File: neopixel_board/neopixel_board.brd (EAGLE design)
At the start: 94 x 86 mm, 64 parts, among them U1 UA7805CKCT, U2 MIC5219, U3 ATMEGA32U4, U4 UA7805CKCT, U5 UA7805CKCT, U6 UA7805CKCT, Y1 16MHz

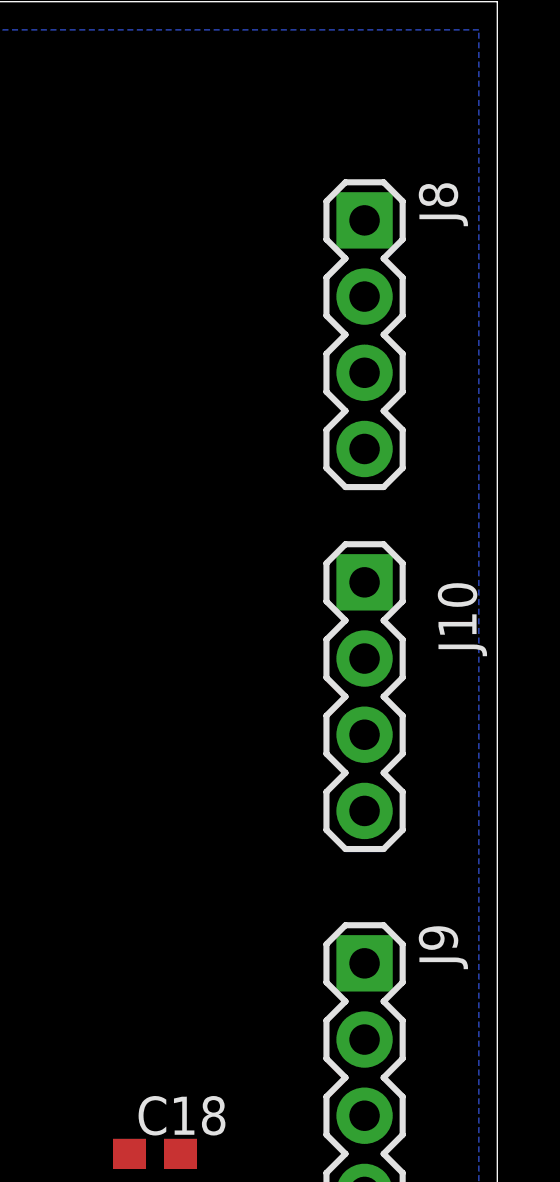
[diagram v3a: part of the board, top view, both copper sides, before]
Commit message: Schematic changes
Named neopixel connectors in order
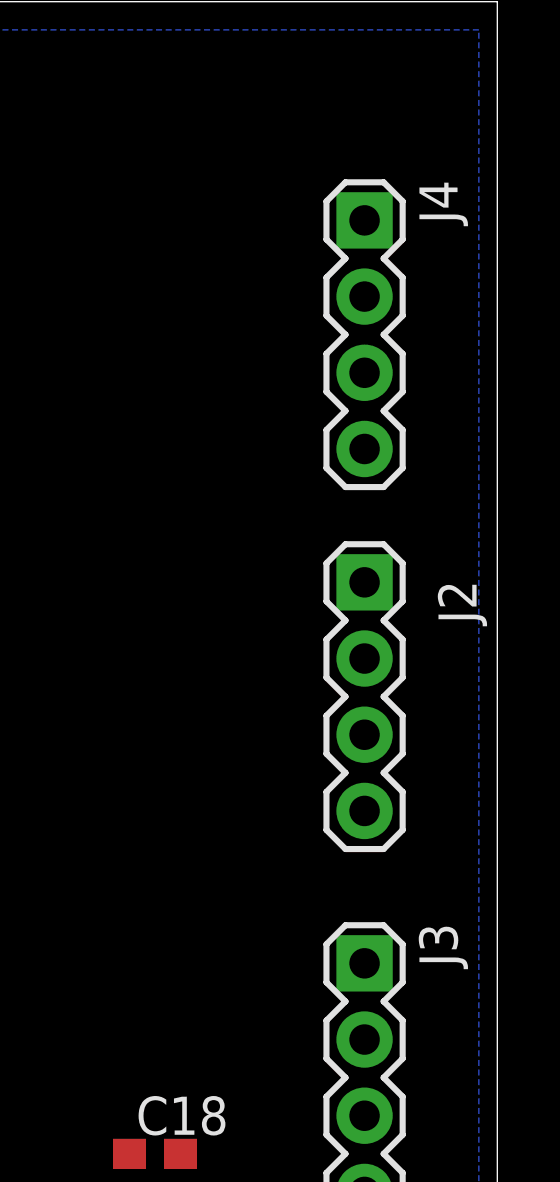
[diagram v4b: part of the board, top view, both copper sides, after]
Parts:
- renumbered J10 to J2, J8 to J4, J9 to J3
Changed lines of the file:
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@@
 <attribute name="VALUE" x="73.406" y="38.989" size="0.4064" layer="27"/>
 </element>
-<element name="J10" library="SparkFun-Connectors" package="1X04" value="" x="89.535" y="66.675" rot="R270">
+<element name="J2" library="SparkFun-Connectors" package="1X04" value="" x="89.535" y="66.675" rot="R270">
 <attribute name="NAME" x="91.9988" y="66.7512" size="1.27" layer="25" ratio="10" rot="R270"/>
 <attribute name="PROD_ID" value="CONN-09696" x="48.895" y="8.255" size="1.778" layer="27" rot="R270" display="off"/>
 <attribute name="VALUE" x="86.36" y="67.945" size="1.27" layer="27" rot="R270"/>
 </element>
-<element name="J8" library="SparkFun-Connectors" package="1X04" value="" x="89.535" y="78.74" rot="R270">
+<element name="J4" library="SparkFun-Connectors" package="1X04" value="" x="89.535" y="78.74" rot="R270">
 <attribute name="NAME" x="91.3638" y="80.0862" size="1.27" layer="25" ratio="10" rot="R270"/>
 <attribute name="PROD_ID" value="CONN-09696" x="48.895" y="43.18" size="1.778" layer="27" rot="R270" display="off"/>
 <attribute name="VALUE" x="86.36" y="80.01" size="1.27" layer="27" rot="R270"/>
 </element>
-<element name="J9" library="SparkFun-Connectors" package="1X04" value="" x="89.535" y="53.975" rot="R270">
+<element name="J3" library="SparkFun-Connectors" package="1X04" value="" x="89.535" y="53.975" rot="R270">
 <attribute name="NAME" x="91.3638" y="55.3212" size="1.27" layer="25" ratio="10" rot="R270"/>
 <attribute name="PROD_ID" value="CONN-09696" x="48.895" y="6.985" size="1.778" layer="27" rot="R270" display="off"/>
@@
 <contactref element="PB1" pad="P$3"/>
 <contactref element="PB1" pad="P$4"/>
-<contactref element="J10" pad="1"/>
-<contactref element="J8" pad="2"/>
-<contactref element="J10" pad="2"/>
-<contactref element="J9" pad="2"/>
-<contactref element="J9" pad="1"/>
-<contactref element="J8" pad="1"/>
+<contactref element="J2" pad="1"/>
+<contactref element="J4" pad="2"/>
+<contactref element="J2" pad="2"/>
+<contactref element="J3" pad="2"/>
+<contactref element="J3" pad="1"/>
+<contactref element="J4" pad="1"/>
 <contactref element="C2" pad="2"/>
 <contactref element="C4" pad="2"/>
@@
 </signal>
 <signal name="VCC2">
-<contactref element="J10" pad="4"/>
+<contactref element="J2" pad="4"/>
 <contactref element="U4" pad="3"/>
 <contactref element="C12" pad="1"/>
@@
 <contactref element="U5" pad="3"/>
 <contactref element="C15" pad="1"/>
-<contactref element="J9" pad="4"/>
+<contactref element="J3" pad="4"/>
 <contactref element="R9" pad="1"/>
 <contactref element="C21" pad="1"/>
@@
 </signal>
 <signal name="VCC4">
-<contactref element="J8" pad="4"/>
+<contactref element="J4" pad="4"/>
 <contactref element="R10" pad="1"/>
 <contactref element="U6" pad="3"/>
@@
 <signal name="N$14">
 <contactref element="R12" pad="1"/>
-<contactref element="J10" pad="3"/>
+<contactref element="J2" pad="3"/>
 <wire x1="89.535" y1="61.595" x2="63.92" y2="31.115" width="0" layer="19" extent="1-1"/>
 </signal>
 <signal name="N$15">
 <contactref element="R13" pad="1"/>
-<contactref element="J9" pad="3"/>
+<contactref element="J3" pad="3"/>
 <wire x1="89.535" y1="48.895" x2="67.095" y2="77.47" width="0" layer="19" extent="1-1"/>
 </signal>
@@
 <signal name="N$3">
 <contactref element="R14" pad="1"/>
-<contactref element="J8" pad="3"/>
+<contactref element="J4" pad="3"/>
 <wire x1="89.535" y1="73.66" x2="63.285" y2="77.47" width="0" layer="19" extent="1-1"/>
 </signal>

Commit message: Board Finished (tentative)
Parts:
- removed C1: 0.1uF, rcl:C0603
- removed C11, C14, C16, C8: 0.1 uF, rcl:C0603
- removed C15, C17, C9: 0.33 uF, rcl:C0603
- removed C20, C21, C22: 1000uF, neopixel_board:PCAP_8X10-ELECT
- removed LD7: GREEN, SparkFun-LED:LED-0603
- removed R13, R14: 470Ω, SparkFun-Resistors:0603
- removed R15: 1kΩ, SparkFun:0603-RES
- removed U1, U4, U5, U6: UA7805CKCT, Training_Board:KC3
- removed U3: ATMEGA32U4, Testing:QFN-44-NOPAD_1:1-OUTFAKES
- removed X1: (no value), Testing:USB-AB-MICRO-SMD-V03-IN&OUT
- removed XF1: 4A, RoboJackets-Fuses:3557-2
- added 5VSOURCE, GND_TERMINAL: THOLE_SOURCE, neopixel_board:THOLE_SOURCE
- added F2, F3, F4: 4A, neopixel_board:3557-2
- added F5: 13A, neopixel_board:3557-2
- added J5: 47589-0001_2, neopixel_board:MOLEX_47589-0001_FIX
- added MCU: 32U4, SparkFun-IC-Microcontroller:TQFP44
- C12: value 0.33 uF -> 1000uF; device rcl:C0603 -> SparkFun:EIA3216
- J1: value (none) -> SSW-102-02-T-S-RA; device SparkFun-Connectors:SCREWTERMINAL-3.5MM-2 -> neopixel_board:CON2_1X2_TR_SSQ
- J2, J3, J4: value (none) -> SSW-102-02-T-S-RA; device SparkFun-Connectors:1X04 -> neopixel_board:CON2_1X2_TR_SSQ
- R12: value 470Ω -> 1kΩ; device SparkFun-Resistors:0603 -> SparkFun:0603-RES
- R4: value 1kΩ -> 470Ω; device SparkFun:0603-RES -> SparkFun-Resistors:0603
- moved J4 96.1 mm to (9.91, 24.9), turned to 90 degrees
- moved J2 82.2 mm to (9.91, 46.4), turned to 90 degrees
- moved J3 79.7 mm to (9.91, 56.3), turned to 90 degrees
- moved C2 76.5 mm to (31.8, 5.08), turned to 90 degrees
- moved R5 70.4 mm to (11.2, 8.76)
- moved C4 69.9 mm to (31.8, 9.53), turned to 270 degrees
- moved R7 67.2 mm to (11.0, 5.97)
- moved C6 66.2 mm to (40.6, 10.4), turned to 90 degrees
- moved C7 66.1 mm to (45.7, 22.6), turned to 270 degrees
- moved R12 62.6 mm to (9.53, 60.6)
- moved R2 58.8 mm to (40.6, 22.6), turned to 270 degrees
- moved D1 58.4 mm to (21.3, 27.9), turned to 180 degrees
- moved LD8 57.8 mm to (36.8, 58.2)
- moved PB2 57.3 mm to (43.3, 16.4)
- moved R8 56.6 mm to (45.7, 10.4), turned to 90 degrees
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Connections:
- removed net AREF: C1.1, U3.42
- removed net N$3: J4.3, R14.1
- removed net NEOPIXEL_1: R13.2, U3.29
- removed net NEOPIXEL_2: R14.2, U3.30
- removed net UVCC: D1.A, X1.VBUS1
- removed net VCC1: C6.1, C9.1, F1.1, R15.1, U1.3, U3.2, U3.7
- removed net VCC2: C12.1, C20.1, J2.4, R4.1, U4.3
- removed net VCC3: C15.1, C21.1, J3.4, R9.1, U5.3
- removed net VCC4: C17.1, C22.1, J4.4, R10.1, U6.3
- removed net VSOURCE: C11.1, C14.1, C16.1, C8.1, R3.2, U1.1, U4.1, U5.1, U6.1, XF1.3, XF1.4
- new net 5VIN: 5VSOURCE.1, F5.1, F5.2
- new net N$17: D1.A, J5.1
- new net N$18: LD3.A, R2.2
- new net VCC_5V: C12.A, F1.1, F2.3, F2.4, F3.3, F3.4, F4.3, F4.4, F5.3, F5.4, R3.2
- net D+: now also MCU.4; no longer U3.4
- net D-: now also MCU.3; no longer U3.3
- net ETH_INT: now also MCU.27; no longer U3.27
- net ETH_MISO: now also MCU.8; no longer U3.8
- net ETH_MOSI: now also MCU.10; no longer U3.10
- net ETH_RST: now also MCU.20; no longer U3.20
- net ETH_SCK: now also MCU.9; no longer U3.9
- net ETH_SCNN: now also MCU.11; no longer U3.11
- net GND: now also C12.C, GND_TERMINAL.1, J5.5, J5.P$3, J5.P$4, J5.P$5, J5.P$6, MCU.15, MCU.23, MCU.33, MCU.35, MCU.42, MCU.43, MCU.5; no longer C1.2, C11.2, C12.2, C14.2, C15.2, C16.2, C17.2, C20.2, C21.2, C22.2, C8.2, C9.2, J2.2, J3.2, J4.2, LD3.A, LD7.C, R2.2, U1.2, U3.15, U3.23, U3.33, U3.35, U3.43, U3.5, U4.2, U5.2, U6.2, X1.GND1
- net MCU_RST: now also MCU.13; no longer U3.13
- net N$1: now also MCU.16; no longer U3.16
- net N$10: now also F2.1, F2.2, J2.2, R9.2; no longer LD7.A, R10.2
- net N$11: now also F3.1, F3.2, J1.2, R10.2; no longer LD4.A, R15.2
- net N$12: now also F4.1, F4.2, J3.2, R12.2; no longer LD5.A, R4.2
- net N$13: now also J4.2, R4.1; no longer LD6.A, R9.2
- net N$14: now also LD4.A; no longer J2.3
- net N$15: now also LD5.A, R10.1; no longer J3.3, R13.1
- net N$16: now also LD6.A, R9.1; no longer J1.2, XF1.1, XF1.2
- net N$2: now also MCU.17; no longer U3.17
- net N$4: now also MCU.6; no longer U3.6
- net N$6: now also J5.2; no longer X1.D-1
- net N$8: now also J5.3; no longer X1.D+1
- net NEOPIXEL_0: now also MCU.31, R4.2; no longer R12.2, U3.31
- net TXLED: now also MCU.22; no longer U3.22
- net VCC1_3.3V: now also C6.1, MCU.14, MCU.2, MCU.24, MCU.34, MCU.44, MCU.7; no longer U3.14, U3.24, U3.34, U3.44
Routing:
- net VCC1_3.3V: track 0.00 -> 134.1 mm, vias 0 -> 4
- net GND: track 0.00 -> 100.9 mm, vias 0 -> 18
- net ETH_RST: track 0.00 -> 51.0 mm, vias 0 -> 8
- net MCU_RST: track 0.00 -> 37.1 mm
- net N$17: track 0.00 -> 31.7 mm, vias 0 -> 2
- net NEOPIXEL_0: track 0.00 -> 28.1 mm, vias 0 -> 2
- net N$4: track 0.00 -> 25.3 mm
- net TXLED: track 0.00 -> 23.3 mm, vias 0 -> 2
- net D-: track 0.00 -> 23.1 mm, vias 0 -> 4
- net RAW: track 0.00 -> 21.0 mm
- net N$1: track 0.00 -> 20.0 mm, vias 0 -> 2
- net ETH_SCNN: track 0.00 -> 17.7 mm, vias 0 -> 2
- net D+: track 0.00 -> 17.2 mm, vias 0 -> 2
- net ETH_MOSI: track 0.00 -> 16.8 mm, vias 0 -> 4
- net N$10: track 0.00 -> 16.5 mm
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- added copper zone on layer 1, net 5VIN
- added copper zone on layer 1, net VCC_5V
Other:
- board size 94 x 86 mm -> 52.6 x 65.8 mm

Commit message: BRD finishing touches
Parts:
- ETH1: device WIZ850io:WIZ850IO -> neopixel_board:WIZ850IO
- J5: value 47589-0001_2 -> 1981584-1; device neopixel_board:MOLEX_47589-0001_FIX -> neopixel_board:TE_1981584-1
- moved R7 7.11 mm to (11.2, 13.1)
- moved J5 3.68 mm to (3.68, 11.0), turned to 270 degrees
- moved 5VSOURCE 2.16 mm to (49.4, 57.9)
- moved GND_TERMINAL 2.16 mm to (49.4, 50.7)
- moved R5 1.40 mm to (11.2, 10.2)
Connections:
- net D+ renamed D_P
- net D- renamed D_N
- net GND: now also J5.10, J5.11, J5.6, J5.7, J5.8, J5.9; no longer J5.P$3, J5.P$4, J5.P$5, J5.P$6
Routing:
- net D_N: track 23.1 -> 14.6 mm, vias 4 -> 0
- net N$17: track 31.7 -> 24.0 mm, vias 2 -> 0
- net VCC1_3.3V: track 134.1 -> 128.6 mm
- net GND: track 100.9 -> 103.9 mm
- net D_P: track 17.2 -> 14.7 mm, vias 2 -> 0
- net ETH_MISO: track 14.4 -> 15.1 mm
- net ETH_INT: track 6.14 -> 5.57 mm
- net ETH_RST: track 51.0 -> 50.5 mm, vias 8 -> 7
- net ETH_MOSI: vias 4 -> 3
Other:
- board size 52.6 x 65.8 mm -> 52.6 x 79 mm
- board text added: "ETH_RST"
- board text added: "MCU_RST"

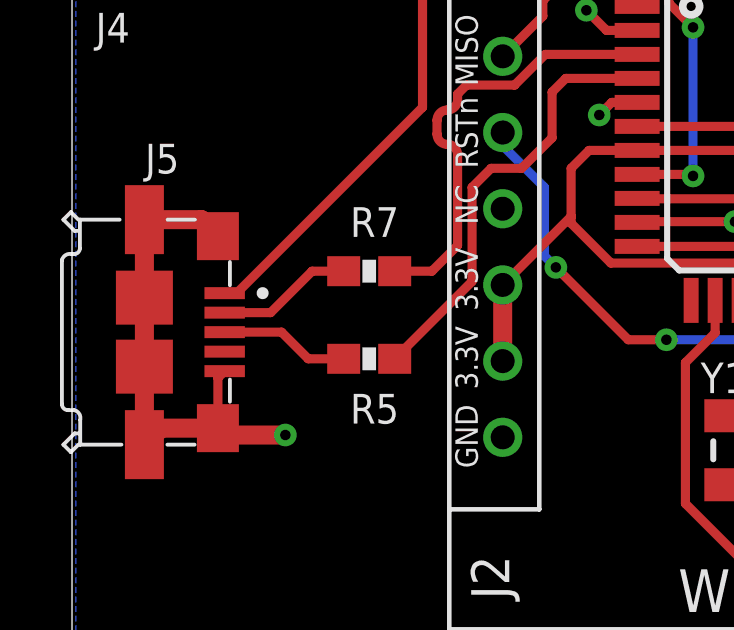
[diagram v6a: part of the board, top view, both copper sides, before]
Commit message: Schematic WIP
addressing W.S. critique
NOTE: in changing voltage tags to symbols, BRD routes are lost
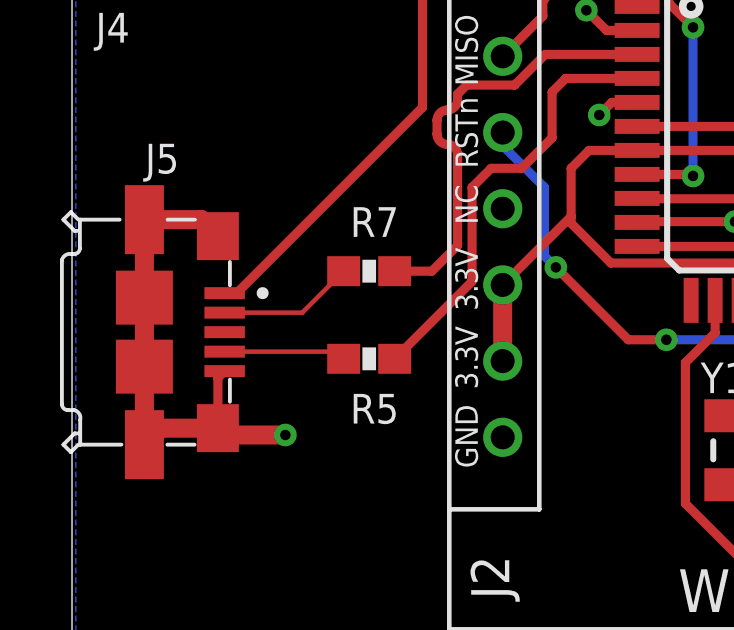
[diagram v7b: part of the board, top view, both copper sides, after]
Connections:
- removed net N$8: J5.3, R5.2
- new net N$3: J5.4, R5.2
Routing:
- net N$8: track 4.34 -> 0.00 mm
- net N$3: track 0.00 -> 4.07 mm
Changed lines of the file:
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@@
 <wire x1="38.989" y1="17.145" x2="35.814" y2="13.97" width="0.3048" layer="1"/>
-</signal>
-<signal name="N$8">
-<contactref element="R5" pad="2"/>
-<contactref element="J5" pad="3"/>
-<wire x1="9.144" y1="10.16" x2="10.326" y2="10.16" width="0.3048" layer="1"/>
-<wire x1="6.358" y1="11.049" x2="8.255" y2="11.049" width="0.3048" layer="1"/>
-<wire x1="8.255" y1="11.049" x2="9.144" y2="10.16" width="0.3048" layer="1"/>
 </signal>
 <signal name="N$7">
@@
 </polygon>
 </signal>
-<signal name="N$6">
-<contactref element="J5" pad="2"/>
-<contactref element="R7" pad="2"/>
-<wire x1="9.271" y1="13.081" x2="10.326" y2="13.081" width="0.3048" layer="1"/>
-<wire x1="6.358" y1="11.699" x2="7.889" y2="11.699" width="0.3048" layer="1"/>
-<wire x1="7.889" y1="11.699" x2="9.271" y2="13.081" width="0.3048" layer="1"/>
-</signal>
 <signal name="N$17">
 <contactref element="D1" pad="A"/>
@@
 <wire x1="14.1224" y1="18.796" x2="14.1224" y2="18.98538125" width="0.3048" layer="1"/>
 </signal>
+<signal name="N$3">
+<contactref element="J5" pad="4"/>
+<contactref element="R5" pad="2"/>
+<wire x1="6.358" y1="10.399" x2="10.087" y2="10.399" width="0.1524" layer="1"/>
+<wire x1="10.087" y1="10.399" x2="10.326" y2="10.16" width="0.1524" layer="1"/>
+</signal>
+<signal name="N$6">
+<contactref element="J5" pad="2"/>
+<contactref element="R7" pad="2"/>
+<wire x1="6.358" y1="11.699" x2="8.944" y2="11.699" width="0.1524" layer="1"/>
+<wire x1="8.944" y1="11.699" x2="10.326" y2="13.081" width="0.1524" layer="1"/>
+</signal>
 </signals>

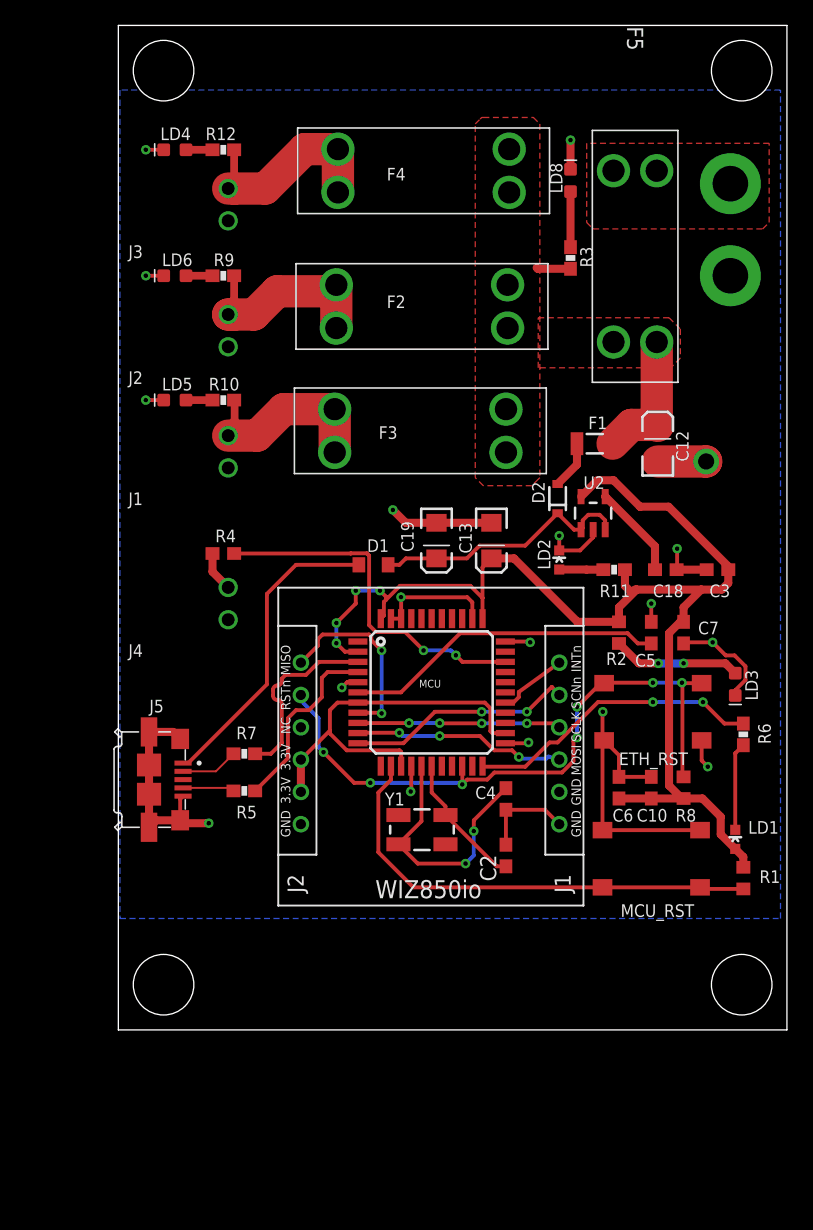
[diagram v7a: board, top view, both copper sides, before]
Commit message: Schematic updates
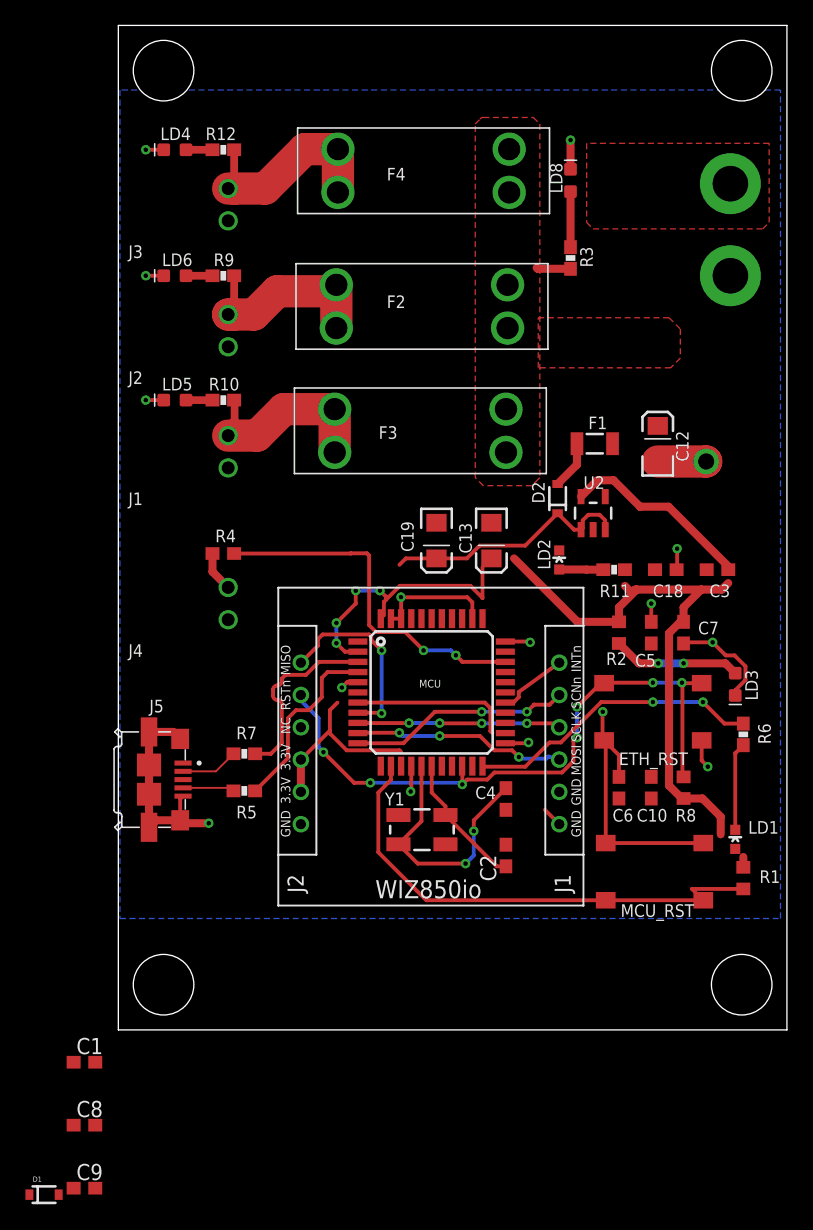
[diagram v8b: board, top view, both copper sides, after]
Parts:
- removed F5: 13A, neopixel_board:3557-2
- added C1, C8, C9: 1uF, rcl:C0603
- D1: device diode:SOD110-W -> SparkFun:SOD-323
- moved D1 55.9 mm to (-4.57, -21.6), turned to 0 degrees
- moved PB1 1.05 mm to (43.4, 3.81)
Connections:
- removed net 5VIN: 5VSOURCE.1, F5.1, F5.2
- removed net VCC1_3.3V: C10.1, C13.A, C3.1, C6.1, C7.1, ETH1.8, ETH1.9, LD1.A, MCU.14, MCU.2, MCU.24, MCU.34, MCU.44, MCU.7, R1.1, R11.2, R2.1, R8.1, U2.5
- removed net VCC_5V: C12.A, F1.1, F2.3, F2.4, F3.3, F3.4, F4.3, F4.4, F5.3, F5.4, R3.2
- new net +3V3: C1.1, C10.1, C13.A, C3.1, C6.1, C7.1, C8.1, C9.1, ETH1.8, ETH1.9, LD1.A, MCU.14, MCU.2, MCU.24, MCU.34, MCU.44, MCU.7, R1.1, R11.2, R2.1, R8.1, U2.5
- new net +5V: 5VSOURCE.1, C12.A, F1.1, F2.3, F2.4, F3.3, F3.4, F4.3, F4.4, R3.2
- net GND: now also C1.2, C8.2, C9.2
- net N$17: now also D1.2; no longer D1.A
- net RAW: now also D1.1; no longer D1.C
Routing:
- net VCC1_3.3V: track 128.6 -> 0.00 mm, vias 4 -> 0
- net +3V3: track 0.00 -> 110.0 mm, vias 0 -> 4
- net N$4: track 25.3 -> 0.00 mm
- net N$17: track 24.0 -> 0.00 mm
- net GND: track 103.9 -> 81.3 mm, vias 18 -> 16
- net VCC_5V: track 13.4 -> 0.00 mm
- net N$5: track 7.37 -> 0.00 mm
- net +5V: track 0.00 -> 2.70 mm
- net MCU_RST: track 37.1 -> 39.6 mm
- net RAW: track 21.0 -> 20.2 mm
- net ETH_SCNN: track 18.0 -> 17.4 mm
